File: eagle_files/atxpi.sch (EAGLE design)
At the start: 9 parts

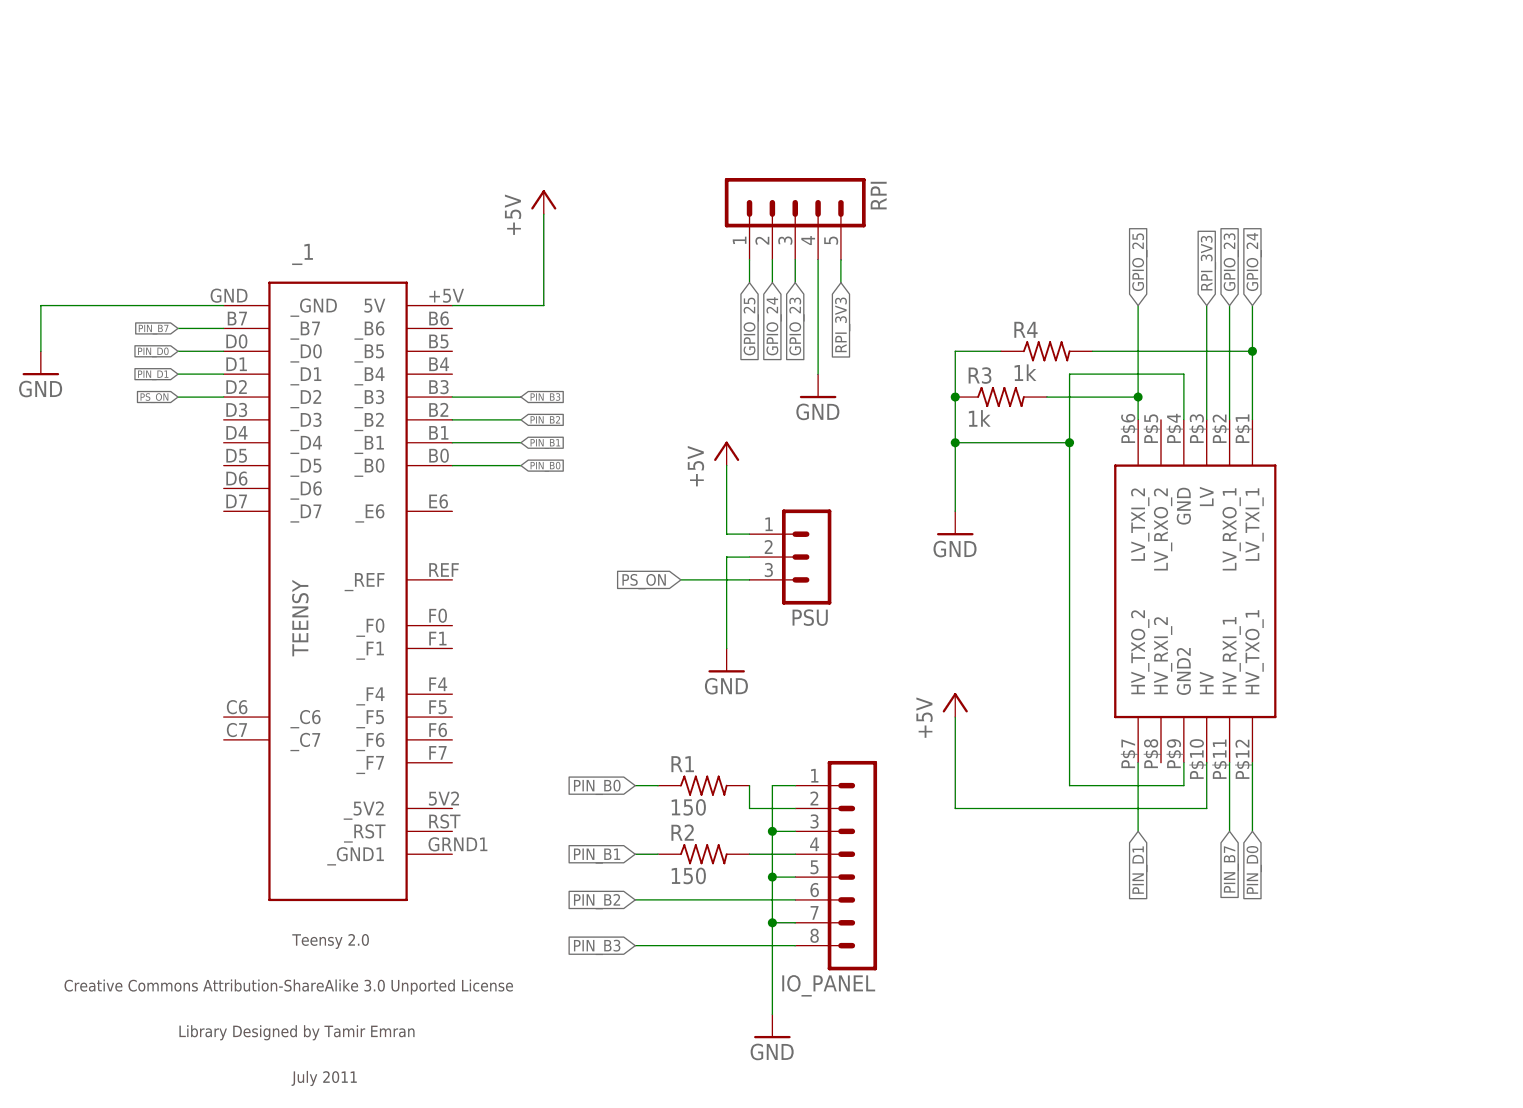
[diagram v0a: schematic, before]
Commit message: add atxpi board
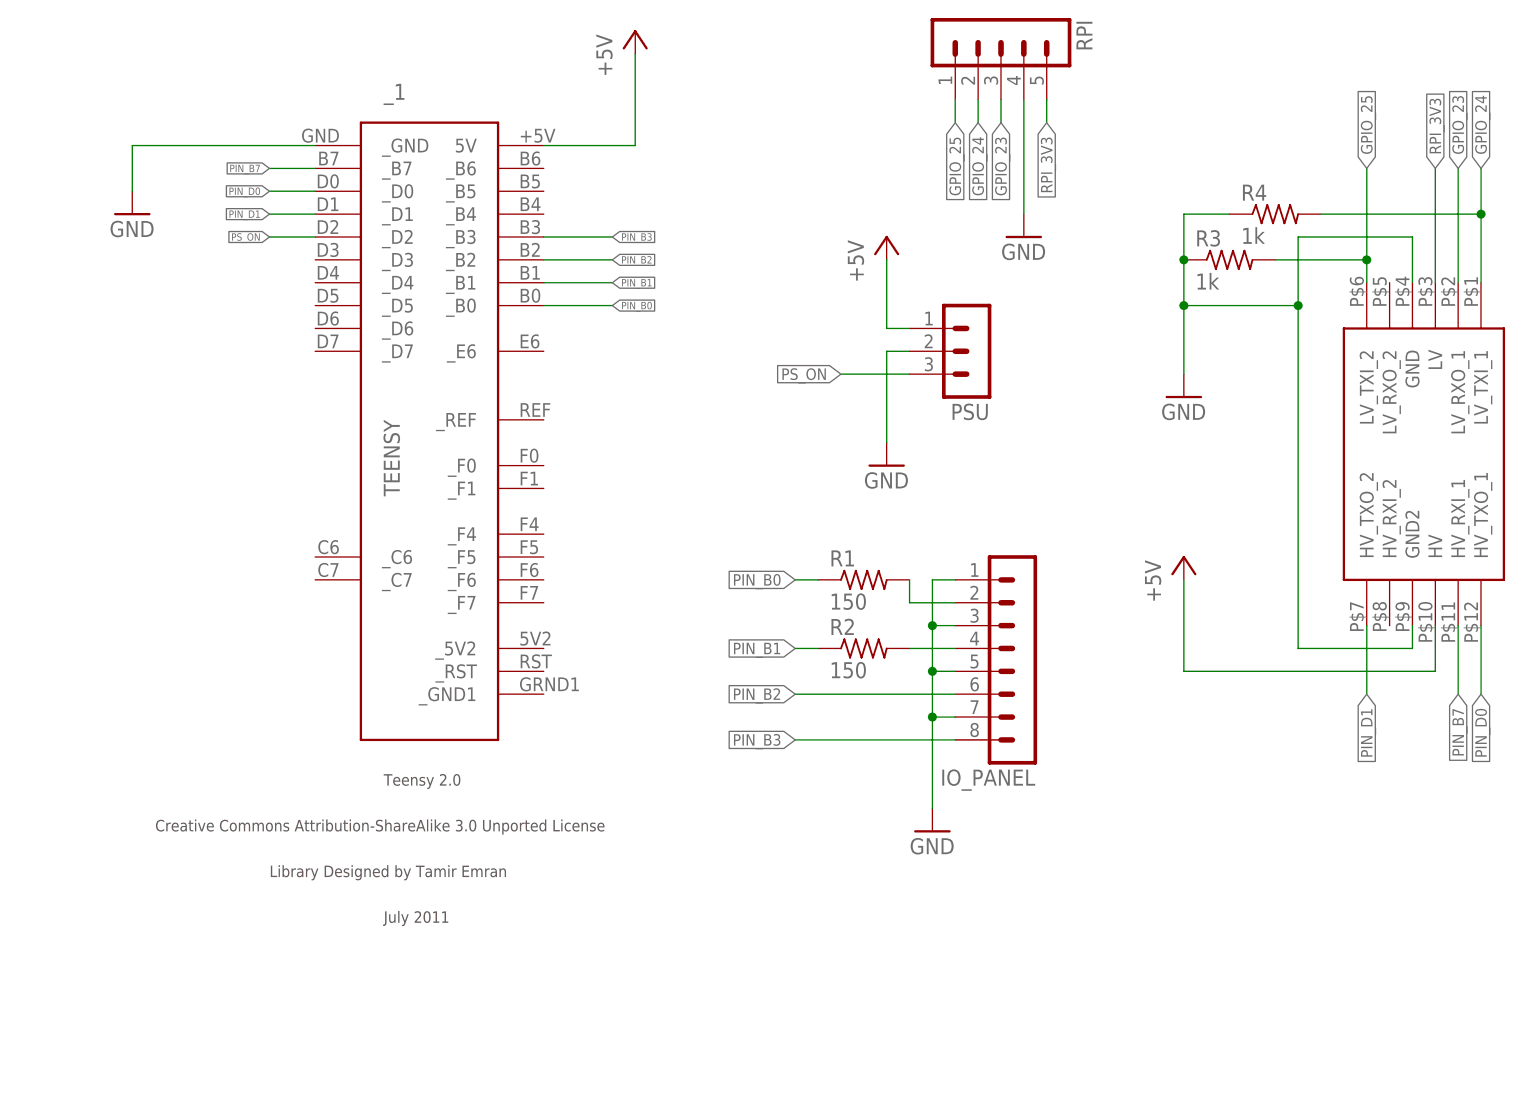
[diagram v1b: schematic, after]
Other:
- moved on the sheet: IO_PANEL, PSU, R1, R2, R3, R4, RPI, _1
